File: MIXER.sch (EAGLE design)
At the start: 109 parts, among them IC1 AD1939WBSTZ, IC10 LM833N, IC11 LM833N, IC2 MCP6004-I_P, IC3 MCP6004-I_P, IC4 LM833N, IC5 LM833N, IC6 LM833N, IC7 LM833N, IC8 LM833N, IC9 LM833N, SW1 EC12E_SW, SW2 EC12E_SW

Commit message: added changes to the control and clock sections
Audio sections to do next
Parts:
- removed IC2: MCP6004-I_P, SamacSys_Parts:MCP6004-I_P
- removed R15: (no value), rcl:R-EU_R0603
- removed U$12, U$8: WQP-PJ301M-12_JACK, thonkiconn:WQP-PJ301M-12_JACK
- removed VR3, VR4, VR5, VR6: 10k, SparkFun-Resistors:POTENTIOMETER-PTH-9MM-1/20W-20%-KIT
- added C34, C35, C36, C37, C38, C39: 1u, rcl:C-EUC0805
- added C40: 5.6n, rcl:C-EUC0805
- added C41: 150p, rcl:C-EUC0805
- added C42, C43: 22p, rcl:C-EUC0805
- added C44: (no value), rcl:C-EUC0805
- added IC12: TL074P, linear:TL074P
- added JP1: (no value), jumper:JP1Q
- added JP2: (no value), jumper:JP2W
- added R33, R37, R39: 200k, rcl:R-EU_R0603
- added R34, R38, R41: 33k, rcl:R-EU_R0603
- added R35, R36, R40: 100k, rcl:R-EU_R0603
- added R42, R43, R44, R45, R46, R47, R48, R49, R50, R51: 10k, rcl:R-EU_R0603
- added R52: 4.3k, rcl:R-EU_R0603
- added R53: (no value), rcl:R-EU_R0603
- added VR7, VR8: 10k, SparkFun-Resistors:POTENTIOMETER-PTH-9MM-1/20W-20%-KIT
- added Y1: 12.288MHz, SparkFun-Clocks:CRYSTAL-12.288MHZ"
- C32, C33: value (none) -> 1u; device rcl:CPOL-EU153CLV-0405 -> rcl:C-EUC0805
- IC3: value MCP6004-I_P -> 24AA1025-I_P; device SamacSys_Parts:MCP6004-I_P -> SamacSys_Parts:24AA1025-I_P
- R12: value (none) -> 100
- R13: value (none) -> 33
- R14: value (none) -> 10k
- R30: value (none) -> 200k
- R31: value (none) -> 33k
- R32: value (none) -> 100k
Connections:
- net N$7 renamed +5V
- net VDD renamed VEE
- new net 1452_CLK_OUT: R13.1
- new net CV0: C32.2, IC12A.OUT, R31.2, U$1G$1.AUXADC0_8
- new net CV1: C33.2, IC12B.OUT, R34.2, U$1G$1.AUXADC1_9
- new net CV2: C34.1, IC12C.OUT, R38.1, U$1G$1.AUXADC2_10
- new net CV3: C35.1, IC12D.OUT, R41.1, U$1G$1.AUXADC3_11
- new net ENCODER0_0: C36.1, R42.2, U$1G$5.MP6_45
- new net ENCODER0_1: C37.1, R43.1, U$1G$5.MP7_46
- new net ENCODER0_2: R50.2, SW1G$2.1, U$1G$4.LRCLK_IN3/MP13_69
- new net ENCODER1_0: C38.1, R46.2, U$1G$2.SS_M/MP0_26
- new net ENCODER1_1: C39.1, R47.1, U$1G$2.MOSI_M/MP1_27
- new net ENCODER1_2: R51.2, SW2G$2.1, U$1G$4.LRCLK_IN2/MP12_66
- new net MOSI: U$1G$2.MOSI/ADDR1_32
- new net N$13: R35.2, U$6.2
- new net N$14: R33.2, VR2.S
- new net N$15: C33.1, IC12B.-IN, R33.1, R34.1, R35.1
- new net N$16: R37.2, VR7.S
- new net N$17: C34.2, IC12C.-IN, R36.1, R37.1, R38.2
- new net N$18: R39.2, VR8.S
- new net N$19: R40.2, U$9.2
- new net N$20: C35.2, IC12D.-IN, R39.1, R40.1, R41.2
- new net N$21: C41.1, U$1G$3.PLLFILT_16
- new net N$22: R42.1, R45.1, SW1G$1.A
- new net N$23: R43.2, R44.1, SW1G$1.B
- new net N$24: C40.1, R52.1
- new net N$25: R46.1, R49.1, SW2G$1.A
- new net N$26: R47.2, R48.1, SW2G$1.B
- new net N$27: R12.2, U$1G$2.XTALOUT_22
- new net N$28: C42.2, R12.1, Y1.1
- new net N$29: C43.2, U$1G$2.MCLK/XTALIN_21, Y1.2
- new net N$30: R13.2, U$1G$2.CLKOUT_23
- new net N$31: JP1.2, U$1G$2.SELFBOOT_34
- new net N$32: JP1.1, R14.1
- new net N$33: IC3.WP, R16.2
- new net N$7: JP2.2, R16.1
- new net RESET: U$1G$2.RESET_24
- new net SCL: U$1G$2.SCLK/SCL_31
- new net SCL_M: IC3.SCL, R53.2, U$1G$2.SCL_M/SCLK_M/MP2_28
- new net SDA: U$1G$2.MISO/SDA_30
- new net SDA_M: IC3.SDA, R17.2, U$1G$2.SDA_M/MISO_M/MP3_29
- new net SS: U$1G$2.SS/ADDR0_33
- new net VSS: IC12A.+IN, IC12B.+IN, IC12C.+IN, IC12D.+IN
- net +3V3: now also C40.2, C41.2, C44.2, IC3.VCC, JP2.3, R14.2, R17.1, R44.2, R45.2, R48.2, R49.2, R50.1, R51.1, R53.1
- net -10V: now also VR2.A, VR7.A, VR8.A
- net GND: now also C36.2, C37.2, C38.2, C39.2, C42.1, C43.1, C44.1, IC3.A0, IC3.A1, IC3.A2!, IC3.VSS, JP2.1, SW1G$1.C, SW1G$2.2, SW2G$1.C, SW2G$2.2, U$5.3, U$6.3, U$7.1, U$7.3, U$9.1, U$9.3, VR2.E, VR7.E, VR8.E; no longer IC2.VDD, IC2.VINA+, IC2.VINB+
- net N$10: now also C32.1, IC12A.-IN; no longer C32.+, IC2.VINA-
- net N$11: now also R36.2, U$7.2; no longer C32.-, IC2.VOUTA, R31.2
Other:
- note added: "1v2"
- note added: "3v2 Digital Supply"
- note added: "5v5 Digital Supply"
- note added: "Rotary Encoders"
- note added: "TODO: Check and set addresses correctly for all ICs"
- note added: "TODO: Figure out the state of MP0 for self boot when multipurpose"
- note added: "TODO: Make decision about display and hook up encoder 1"
- note added: "TODO: Must remember to place the missing supply pins for the TL074 Must make 1v2 with voltage ref diode thing Must make 10v with voltage ref diode thing"
- note added: "This circuit is Biased by VSS at ~1v2 to give a 0 <> 3v3 signal"
- note added: "VEE is 1v2 for the DSP"
- note added: "VSS is also 1.2, but for an analog use as opposed to digital"
- moved on the sheet: R10, R11, R18, R19, R20, R21, R22, R23, R24, R25, R26, R27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

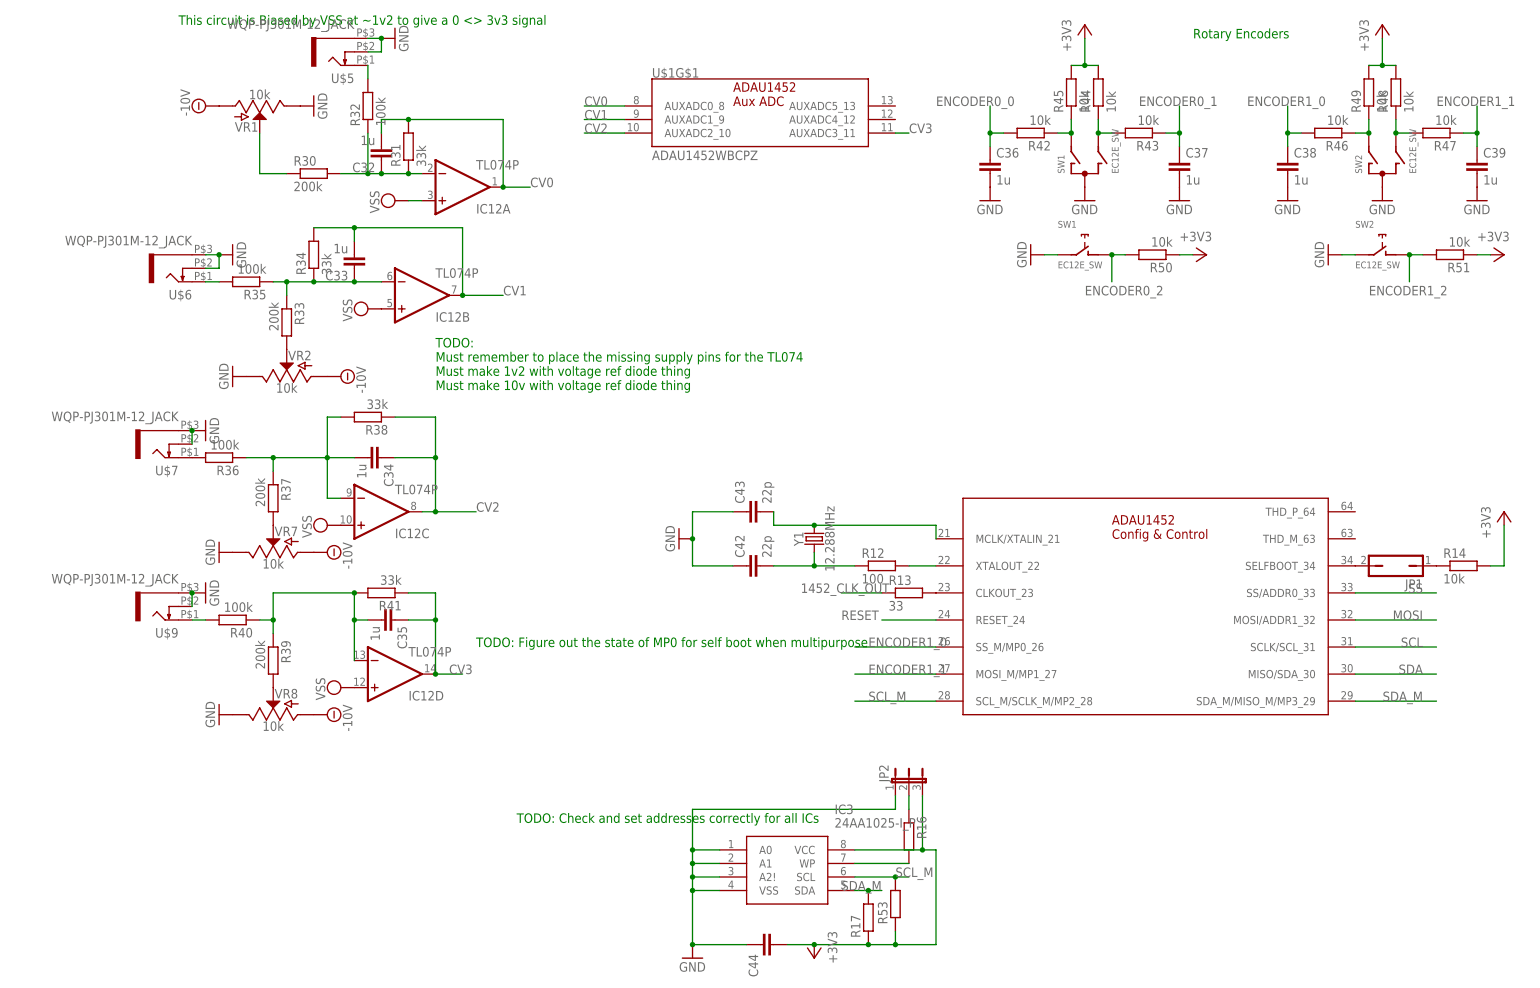
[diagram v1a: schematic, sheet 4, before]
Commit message: im going to have to make it 2 projects to fit the pcb size limits
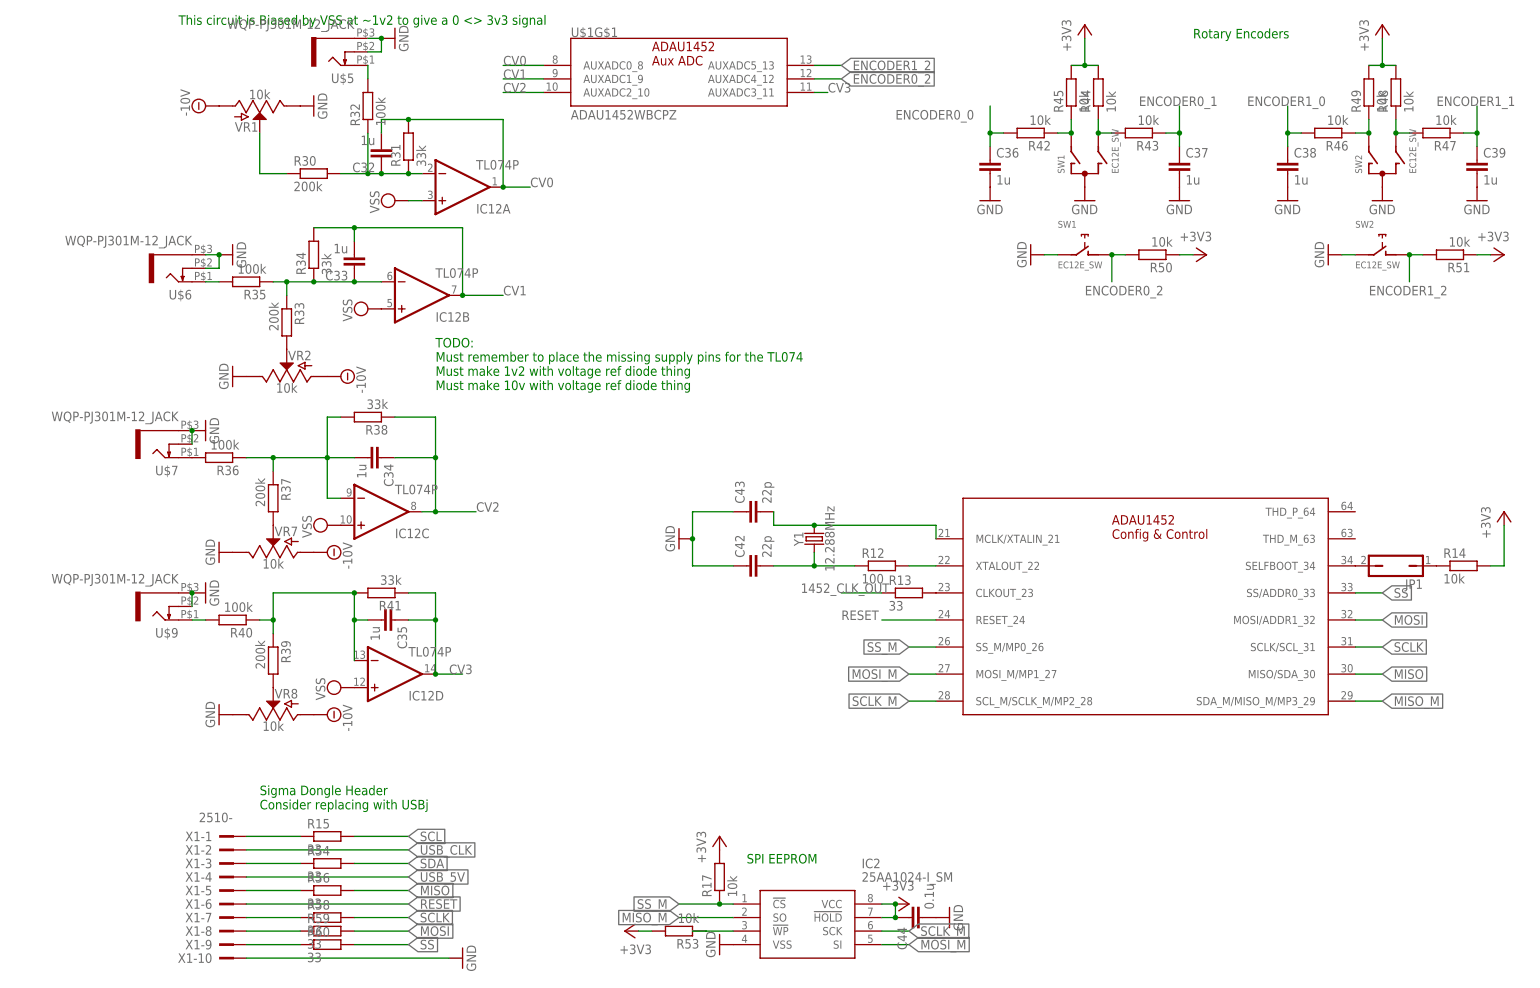
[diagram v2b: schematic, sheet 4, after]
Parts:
- removed IC3: 24AA1025-I_P, SamacSys_Parts:24AA1025-I_P
- removed JP2: (no value), jumper:JP2W
- removed R16: (no value), rcl:R-EU_R0603
- added IC2: 25AA1024-I_SM, SamacSys_Parts:25AA1024-I_SM
- added R15, R54, R56, R58, R59, R60: 33, rcl:R-EU_R0603
- added X1: 2510-, con-3m:2510-
- C44: value (none) -> 0.1u
- R17, R53: value (none) -> 10k
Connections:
- removed net SCL_M: IC3.SCL, R53.2, U$1G$2.SCL_M/SCLK_M/MP2_28
- removed net SDA_M: IC3.SDA, R17.2, U$1G$2.SDA_M/MISO_M/MP3_29
- new net MISO: R56.2, U$1G$2.MISO/SDA_30
- new net MISO_M: IC2.SO, U$1G$2.SDA_M/MISO_M/MP3_29
- new net MOSI_M: IC2.SI, U$1G$2.MOSI_M/MP1_27
- new net N$35: R54.1, X1-3.KL
- new net N$37: R56.1, X1-5.KL
- new net N$39: R58.1, X1-7.KL
- new net N$40: R59.1, X1-8.KL
- new net N$41: R60.1, X1-9.KL
- new net SCLK: R58.2, U$1G$2.SCLK/SCL_31
- new net SCLK_M: IC2.SCK, U$1G$2.SCL_M/SCLK_M/MP2_28
- new net SS_M: IC2.!CS, R17.1, U$1G$2.SS_M/MP0_26
- new net USB_5V: X1-4.KL
- new net USB_CLK: X1-2.KL
- net +3V3: now also C44.1, IC2.!HOLD, IC2.VCC, R17.2, R53.2; no longer C44.2, IC3.VCC, JP2.3, R17.1, R53.1
- net ENCODER0_2: now also U$1G$1.AUXADC4_12; no longer U$1G$4.LRCLK_IN3/MP13_69
- net ENCODER1_0: now also U$1G$4.LRCLK_IN2/MP12_66; no longer U$1G$2.SS_M/MP0_26
- net ENCODER1_1: now also U$1G$4.LRCLK_IN3/MP13_69; no longer U$1G$2.MOSI_M/MP1_27
- net ENCODER1_2: now also U$1G$1.AUXADC5_13; no longer U$1G$4.LRCLK_IN2/MP12_66
- net GND: now also C44.2, IC2.VSS, X1-10.KL; no longer C44.1, IC3.A0, IC3.A1, IC3.A2!, IC3.VSS, JP2.1
- net MOSI: now also R59.2
- net N$33: now also R15.1, X1-1.KL; no longer IC3.WP, R16.2
- net N$7: now also IC2.!WP, R53.1; no longer JP2.2, R16.1
- net RESET: now also X1-6.KL
- net SCL: now also R15.2; no longer U$1G$2.SCLK/SCL_31
- net SDA: now also R54.2; no longer U$1G$2.MISO/SDA_30
- net SS: now also R60.2
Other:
- note added: "SPI EEPROM"
- note added: "Sigma Dongle Header Consider replacing with USBj"
- note removed: "TODO: Check and set addresses correctly for all ICs"
- note removed: "TODO: Figure out the state of MP0 for self boot when multipurpose"
- note removed: "TODO: Make decision about display and hook up encoder 1"
- moved on the sheet: C44, R10, R11, R17, R53, R6, R7, R8, R9, U$1G$1, U$1G$4
